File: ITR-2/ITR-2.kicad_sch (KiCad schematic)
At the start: 8 parts, among them X1 ico*группа_монтажных_отв.&1шт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, X2 ico*группа_монтажных_отв.&1шт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, X3 ico*группа_монтажных_отв.&1шт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, X4 ico*группа_монтажных_отв.&1шт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

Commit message: Т-образная плата с повторителем и контроле напряжения на ОУ
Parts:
- added C1, C2: smd-конденсатор-керамика*0,01мк*25В*0603*ВП, MOTOR_RLC:Конденсатор_SMD_IEC_0603, symbol niisk_lib:smd-конденсатор-керамика*0,01мк*25В*0603*ВП
- added DA1: ОУ*сдвоенный*so-8*ОТК, MOTOR_IMPORT_OTK:SO-8, symbol niisk_lib:ОУ*сдвоенный*so-8*ОТК
- added HL2: smd-светодиод*красный*10мА*0603*ВП, MOTOR_VD_VT_HL:Светодиод_SMD_IEC_0603(AK), symbol niisk_lib:smd-светодиод*красный*10мА*0603*ВП
- added R2, R7: smd-резистор*4,7к*0603*ВП, KICAD6_RLC:Резистор_SMD_IEC_0603-0,1_Вт, symbol niisk_lib_R:smd-резистор*4,7к*0,1Вт*5проц*0603*ВП
- added R3, R5, R6: smd-резистор*10к*0,1Вт*5проц*0603*ВП, KICAD6_RLC:Резистор_SMD_IEC_0603-0,1_Вт, symbol niisk_lib_R:smd-резистор*10к*0,1Вт*5проц*0603*ВП
- added VD1, VD2: smd-стабилитрон*6,8В*5мА*КД-36*ОТК, MOTOR_VD_VT_HL:Корпус_IEC_КД-36, symbol niisk_lib_V:smd-стабилитрон*6,8В*5мА*КД-36*ОТК
- added VT1: smd-транзистор*pnp*0,5А*50В*КТ-46*ОТК, MOTOR_VD_VT_HL:Корпус_КТ-46, symbol niisk_lib:smd-транзистор*pnp*0,5А*50В*КТ-46*ОТК
- HL1: NAME (none) -> Индикатор ИПД169А9-Л АЕЯР.432220.765 ТУ; SUPPLIER (none) -> АО "Протон", г. Орел; ЭКБ (none) -> 2021
- R1: renamed from R2; footprint MOTOR_RLC:Резистор_SMD_IEC_0603-0,075_Вт -> KICAD6_RLC:Резистор_SMD_IEC_0603-0,1_Вт; symbol niisk_lib:smd-резистор*4,7к*0603*ВП -> niisk_lib_R:smd-резистор*4,7к*0,1Вт*5проц*0603*ВП; NAME (none) -> Резистор Р1-12-0,1 ум.-4,7 кОм+-5проц.-Н-«А» ШКАБ.434110.00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; SUPPLIER (none) -> АО "РЕСУРС"; SYMBOL (none) -> 2.728; ЭКБ (none) -> 2021
- renumbered R1 to R4
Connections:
- net 9V-IN: now also SB1.1; no longer SB1.2
- net GND: now also R4.1, C1.1, C2.1, DA1.4, HL2.K, R6.1, VD1.A; no longer R4.3
- net AREF: now reaches R4.2
- net AREF: now also DA1.6; no longer X3.1
- new net: HL2.A, R2.2
- new net: R7.1, VD2.A
- new net: VD2.K, VT1.1
- new net 2V5: DA1.3, R3.1, VD1.K
- new net 9V: C1.2, DA1.8, R1.1, R3.2, R4.3, R5.2, SB1.2, VT1.2
- new net ALARM-LED: DA1.1, R2.1
- new net DIRECT: DA1.7, R7.2
- new net SENS: DA1.2, R5.1, R6.2
- new net UOUT: C2.2, DA1.5, VT1.3, X3.1
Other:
- note removed: "VOUT"
- moved on the sheet: R1, R4, SB1, X1, X2, X3, X4

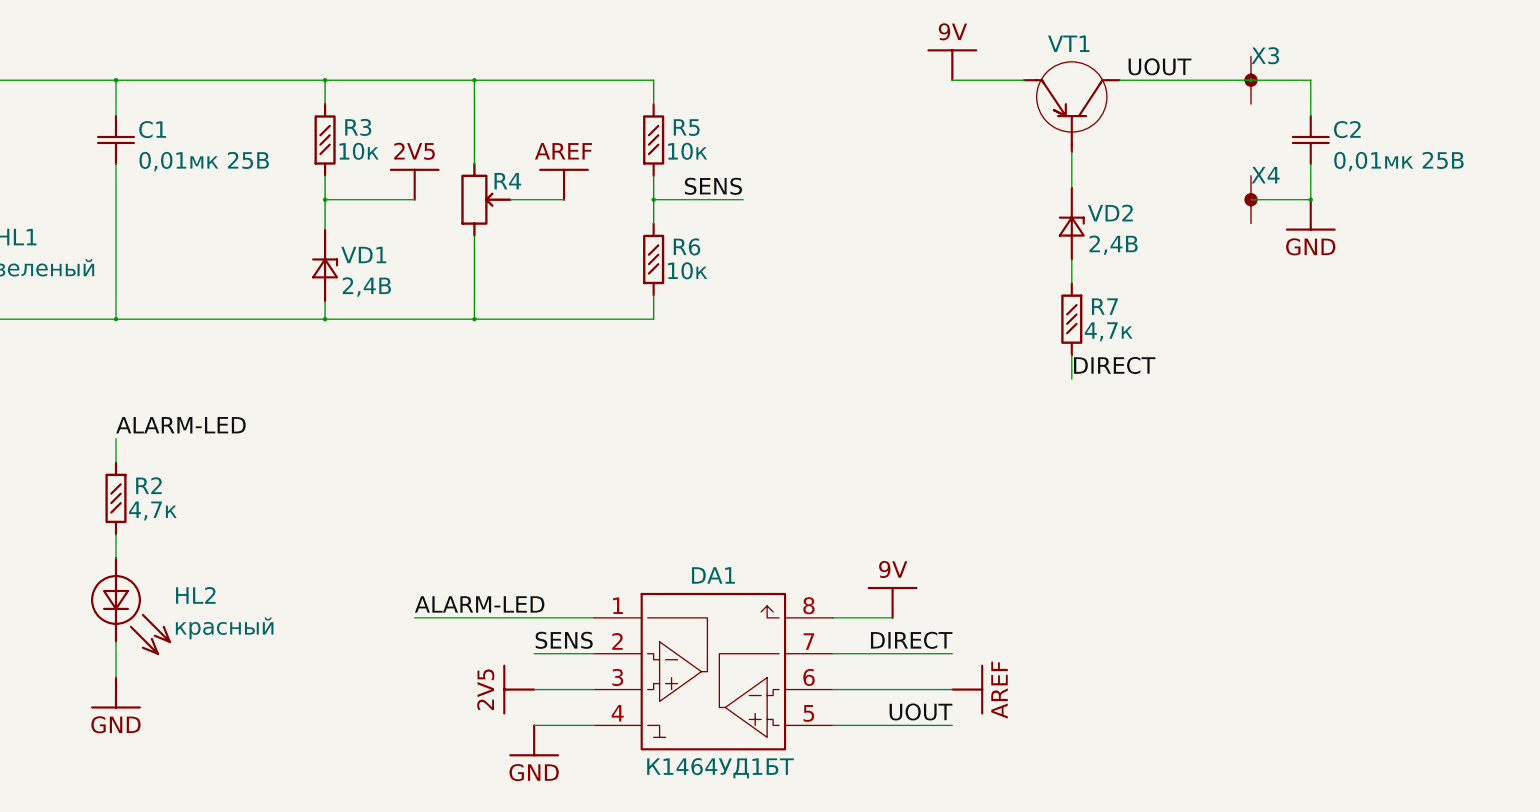
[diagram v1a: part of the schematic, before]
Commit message: исправления по результатам заказа: подтяжки на VT и Uout
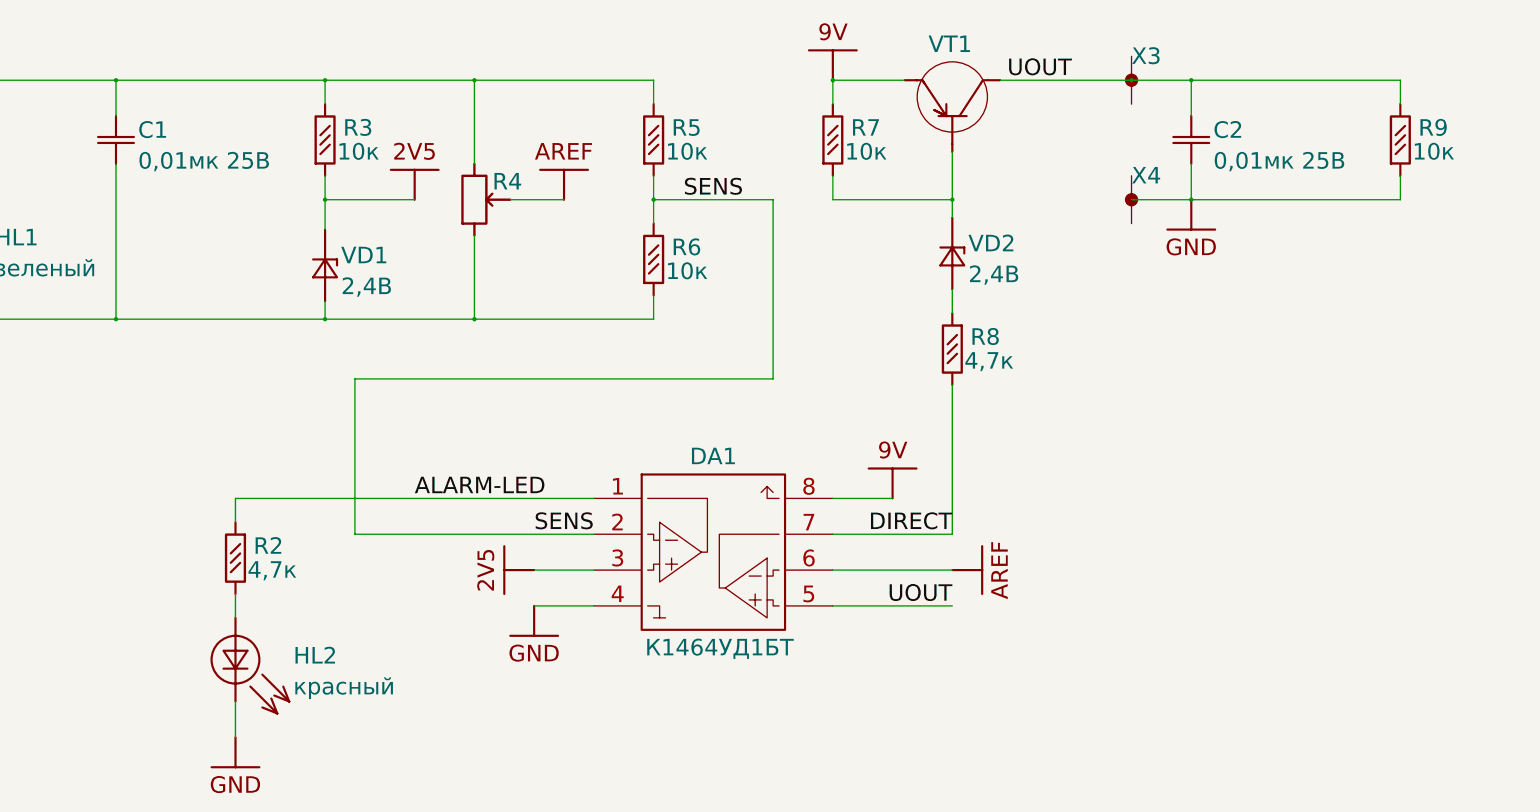
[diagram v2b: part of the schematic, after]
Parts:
- added R7, R9: smd-резистор*10к*0,1Вт*5проц*0603*ВП, KICAD6_RLC:Резистор_SMD_IEC_0603-0,1_Вт, symbol niisk_lib_R:smd-резистор*10к*0,1Вт*5проц*0603*ВП
- renumbered R7 to R8
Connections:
- net 9V: now also R7.2
- net GND: now also R9.1
- net UOUT: now also R9.2
- net at VD2.K, VT1.1: now also R7.1
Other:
- moved on the sheet: C2, DA1, HL2, R2, R8, VD2, VT1, X3, X4

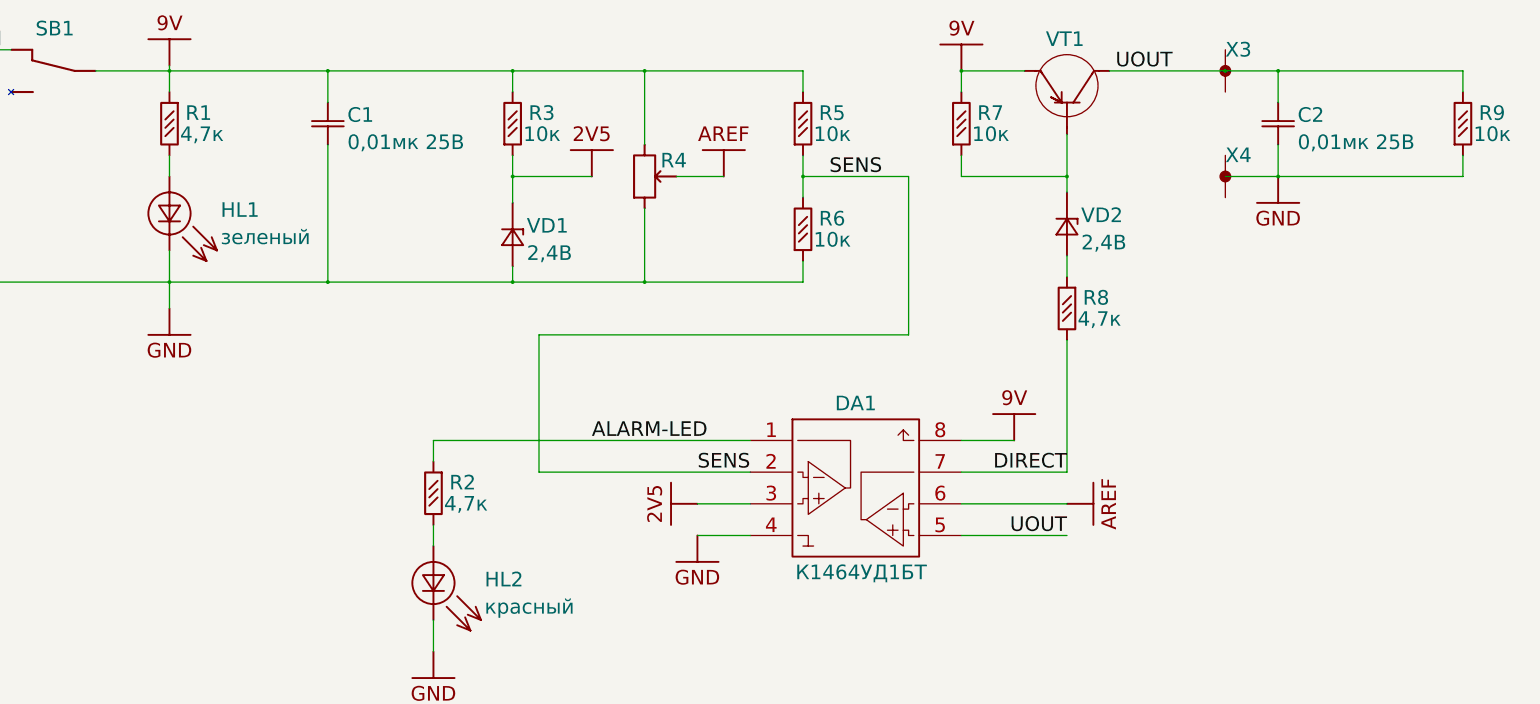
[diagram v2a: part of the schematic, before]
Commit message: инициирована подготовка КД (СПСБ и производственных файлов)
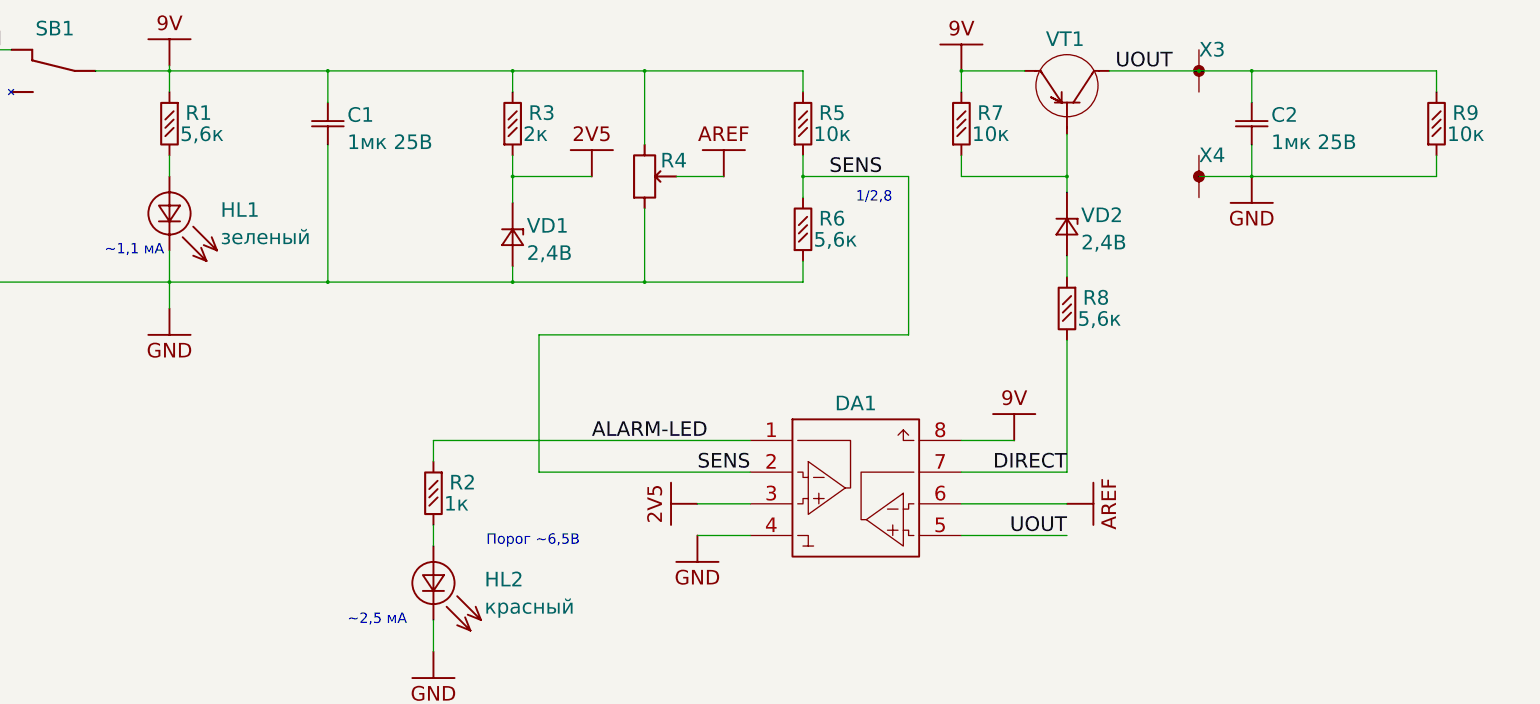
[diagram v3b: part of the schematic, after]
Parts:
- C1, C2: INFO 0,01мк 25В -> 1мк 25В; NAME Конденсатор К10-83-25В-0,01мкФ+-10проц.-Н30 АЖЯР.673511.008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 -> Конденсатор керамический 1 мкФ 10проц. 25В 0603
- DA1: NAME К1464УД1БТ -> Микросхема ОУ LM358ADR
- HL1: NAME Индикатор ИПД169А9-Л АЕЯР.432220.765 ТУ -> Светодиод зеленый GNL-0603GC
- HL2: NAME Индикатор ИПД169А9-К АЕЯР.432220.765 ТУ -> Светодиод красный GNL-0603EC
- R1, R8: INFO 4,7к -> 5,6к; NAME Резистор Р1-12-0,1 ум.-4,7 кОм+-5проц.-Н-«А» ШКАБ.434110.00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 -> Резистор 5,6 кОм 5проц. 0603
- R2: INFO 4,7к -> 1к; NAME Резистор Р1-12-0,1 ум.-4,7 кОм+-5проц.-Н-«А» ШКАБ.434110.00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 -> Резистор 1 кОм 5проц. 0603
- R3: INFO 10к -> 2к; NAME Резистор Р1-12-0,1 ум.-10 кОм+-5проц.-Н-«А» ШКАБ.434110.002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 -> Резистор 2 кОм 5проц. 0603
- R4: NAME (none) -> Резистор переменный R1001N12B1-A10K
- R5, R7, R9: NAME Резистор Р1-12-0,1 ум.-10 кОм+-5проц.-Н-«А» ШКАБ.434110.002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 -> Резистор 10 кОм 5проц. 0603
- R6: INFO 10к -> 5,6к; NAME Резистор Р1-12-0,1 ум.-10 кОм+-5проц.-Н-«А» ШКАБ.434110.002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 -> Резистор 5,6 кОм 5проц. 0603
- SB1: NAME (none) -> Переключатель движковый KLS7-SS-12F19-G5
- VD1, VD2: NAME Стабилитрон 2С4005А91 АЕЯР.432120.780 ТУ -> Стабилитрон BZT52C2V4
- VT1: NAME Транзистор_КТ228Г9 -> Транзистор PNP КТ228Г9 (или ВС807-40)
- X1, X2, X3, X4: INFO (none) -> pcb
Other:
- note added: "1/2,8"
- note added: "~1,1 мА"
- note added: "~2,5 мА"
- note added: "Порог ~6,5В"
- moved on the sheet: C2, R9, X3, X4
